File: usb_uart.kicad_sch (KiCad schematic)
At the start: 13 parts, among them J9 Conn_01x04_Female, U20 CP2102N-A01-GQFN28, U25 CM1293A-04SO

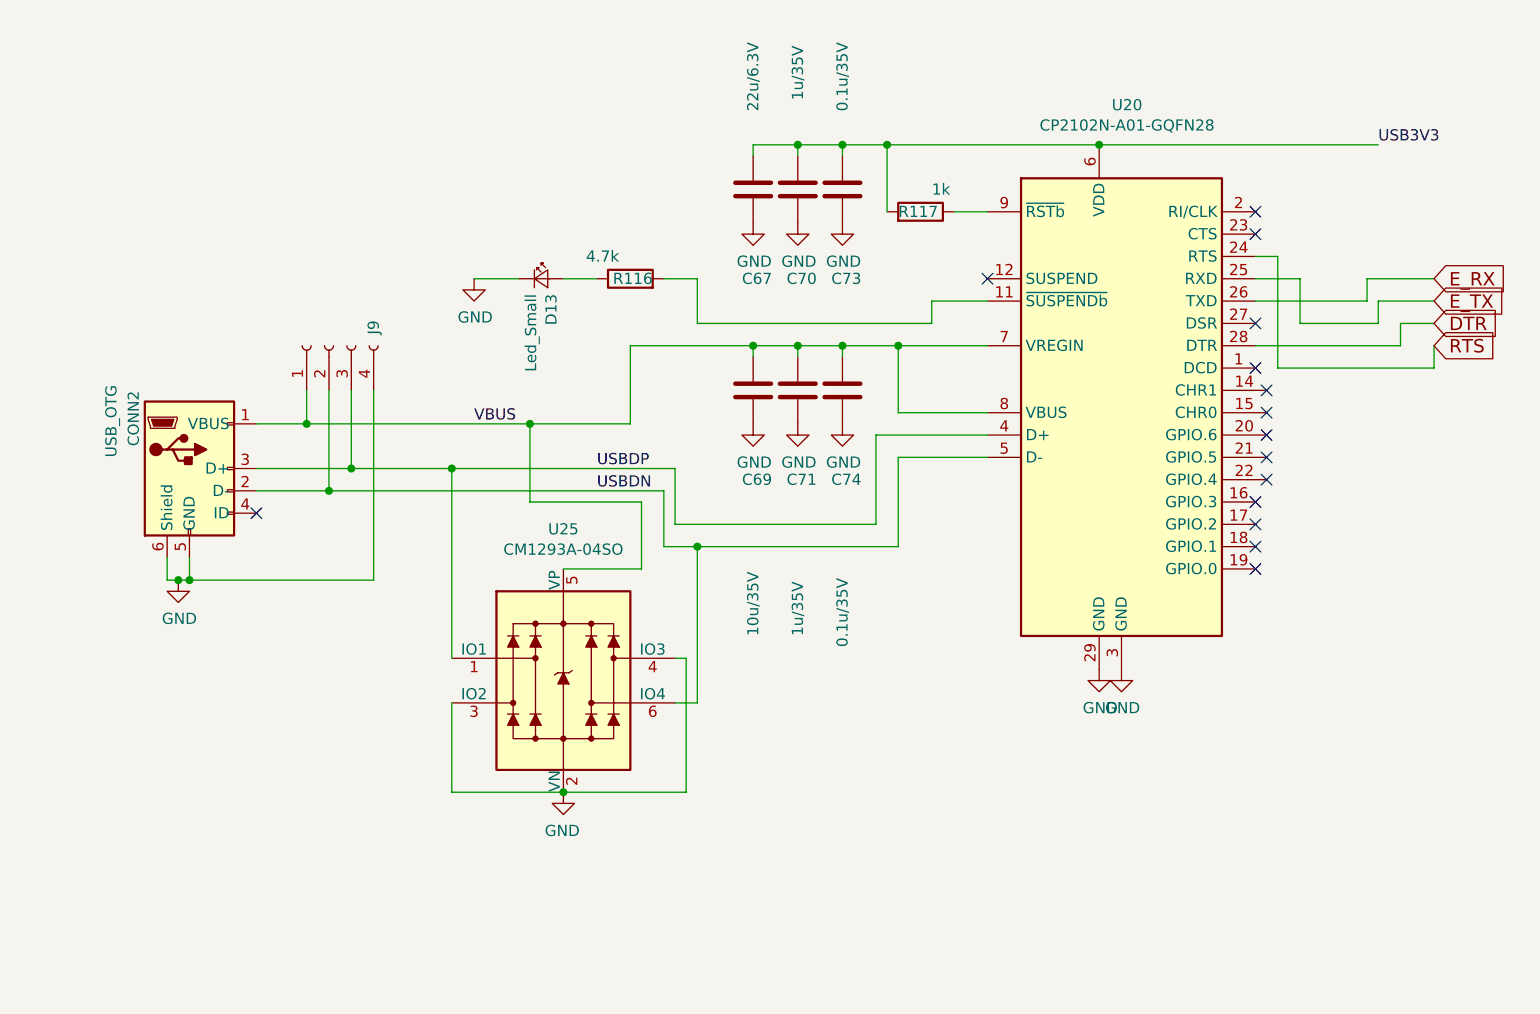
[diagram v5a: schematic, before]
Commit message: WROOM32 coupling capacitor order fixed; Added FB on long line to board left-most sensors
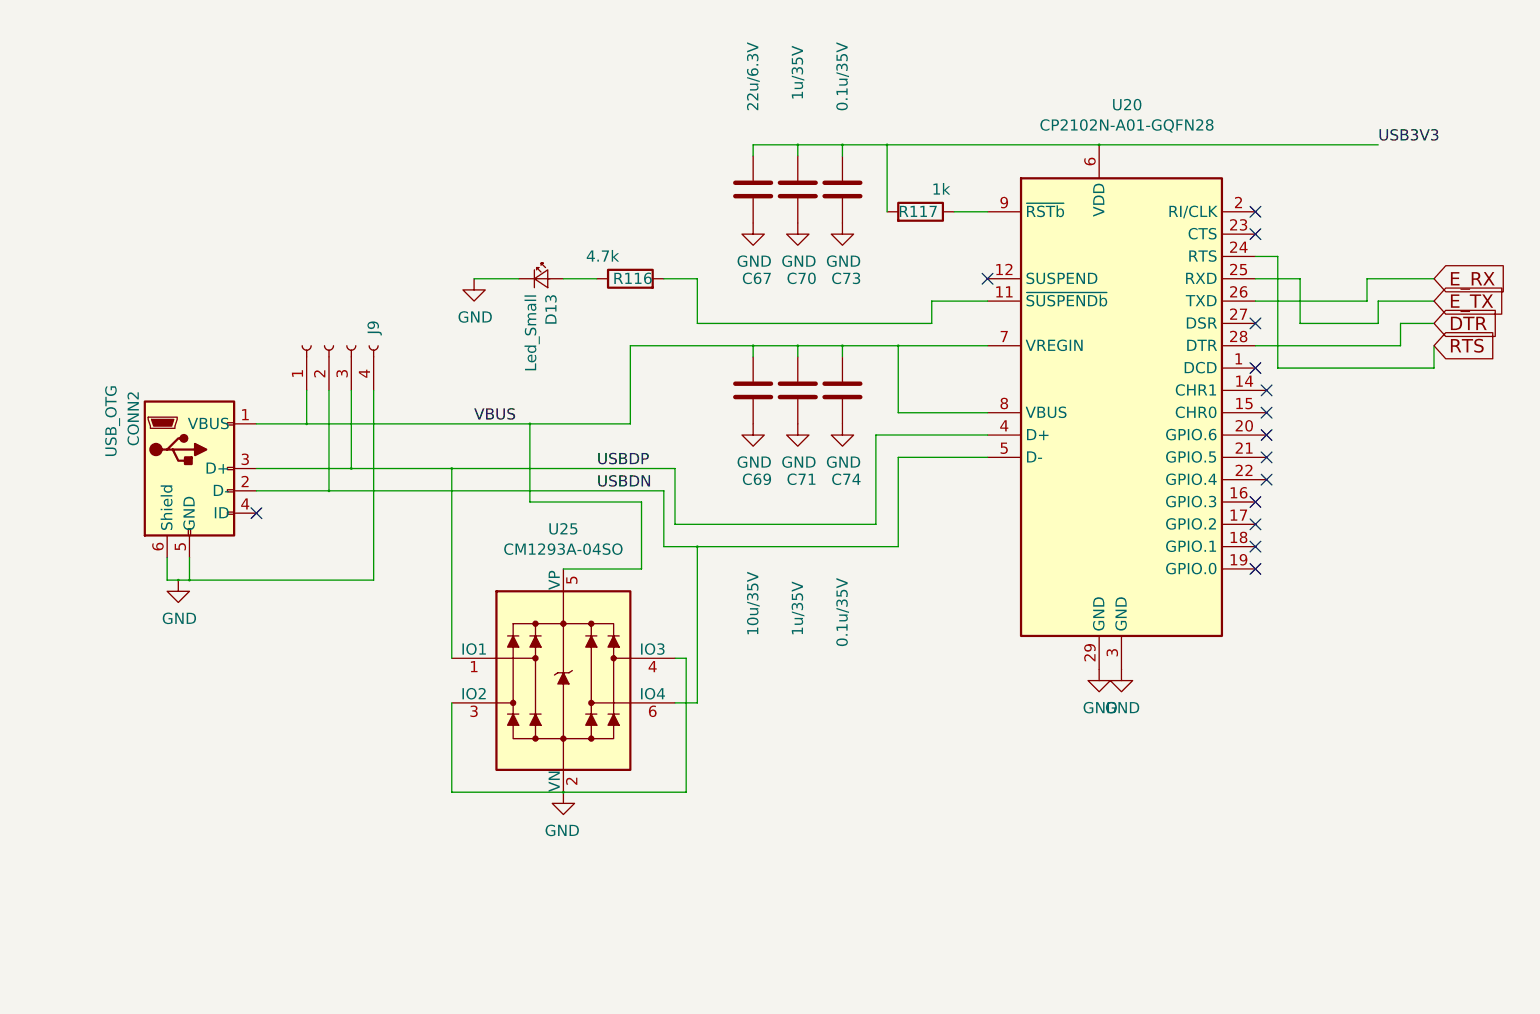
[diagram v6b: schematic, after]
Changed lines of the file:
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@@
-(kicad_sch (version 20200618) (host eeschema "5.99.0-unknown-7340c97~89~ubuntu18.04.1")
-  (page 1 10)
+(kicad_sch (version 20200714) (host eeschema "5.99.0-unknown-e5f2015a9~89~ubuntu18.04.1")
+  (page 10 10)
   (paper "A4")
-  (junction (at 31.115 81.28) (diameter 0) (color 0 0 0 0))
-  (junction (at 32.385 81.28) (diameter 0) (color 0 0 0 0))
-  (junction (at 45.72 63.5) (diameter 0) (color 0 0 0 0))
-  (junction (at 48.26 71.12) (diameter 0) (color 0 0 0 0))
-  (junction (at 50.8 68.58) (diameter 0) (color 0 0 0 0))
-  (junction (at 62.23 68.58) (diameter 0) (color 0 0 0 0))
-  (junction (at 71.12 63.5) (diameter 0) (color 0 0 0 0))
-  (junction (at 74.93 105.41) (diameter 0) (color 0 0 0 0))
-  (junction (at 90.17 77.47) (diameter 0) (color 0 0 0 0))
-  (junction (at 96.52 54.61) (diameter 0) (color 0 0 0 0))
-  (junction (at 101.6 31.75) (diameter 0) (color 0 0 0 0))
-  (junction (at 101.6 54.61) (diameter 0) (color 0 0 0 0))
-  (junction (at 106.68 31.75) (diameter 0) (color 0 0 0 0))
-  (junction (at 106.68 54.61) (diameter 0) (color 0 0 0 0))
-  (junction (at 111.76 31.75) (diameter 0) (color 0 0 0 0))
-  (junction (at 113.03 54.61) (diameter 0) (color 0 0 0 0))
-  (junction (at 135.89 31.75) (diameter 0) (color 0 0 0 0))
+  (junction (at 31.115 81.28) (diameter 0.3048) (color 0 0 0 0))
+  (junction (at 32.385 81.28) (diameter 0.3048) (color 0 0 0 0))
+  (junction (at 45.72 63.5) (diameter 0.3048) (color 0 0 0 0))
+  (junction (at 48.26 71.12) (diameter 0.3048) (color 0 0 0 0))
+  (junction (at 50.8 68.58) (diameter 0.3048) (color 0 0 0 0))
+  (junction (at 62.23 68.58) (diameter 0.3048) (color 0 0 0 0))
+  (junction (at 71.12 63.5) (diameter 0.3048) (color 0 0 0 0))
+  (junction (at 74.93 105.41) (diameter 0.3048) (color 0 0 0 0))
+  (junction (at 90.17 77.47) (diameter 0.3048) (color 0 0 0 0))
+  (junction (at 96.52 54.61) (diameter 0.3048) (color 0 0 0 0))
+  (junction (at 101.6 31.75) (diameter 0.3048) (color 0 0 0 0))
+  (junction (at 101.6 54.61) (diameter 0.3048) (color 0 0 0 0))
+  (junction (at 106.68 31.75) (diameter 0.3048) (color 0 0 0 0))
+  (junction (at 106.68 54.61) (diameter 0.3048) (color 0 0 0 0))
+  (junction (at 111.76 31.75) (diameter 0.3048) (color 0 0 0 0))
+  (junction (at 113.03 54.61) (diameter 0.3048) (color 0 0 0 0))
+  (junction (at 135.89 31.75) (diameter 0.3048) (color 0 0 0 0))
+  (no_connect (at 153.67 72.39))
+  (no_connect (at 123.19 46.99))
+  (no_connect (at 154.94 69.85))
+  (no_connect (at 153.67 57.15))
+  (no_connect (at 153.67 80.01))
+  (no_connect (at 153.67 77.47))
+  (no_connect (at 153.67 52.07))
+  (no_connect (at 154.94 64.77))
+  (no_connect (at 153.67 39.37))
+  (no_connect (at 153.67 74.93))
+  (no_connect (at 154.94 62.23))
   (no_connect (at 154.94 67.31))
-  (no_connect (at 153.67 77.47))
   (no_connect (at 154.94 59.69))
-  (no_connect (at 153.67 39.37))
-  (no_connect (at 153.67 80.01))
-  (no_connect (at 153.67 57.15))
   (no_connect (at 40.005 73.66))
   (no_connect (at 153.67 41.91))
-  (no_connect (at 153.67 74.93))
-  (no_connect (at 154.94 69.85))
-  (no_connect (at 153.67 72.39))
-  (no_connect (at 153.67 52.07))
-  (no_connect (at 154.94 64.77))
-  (no_connect (at 123.19 46.99))
-  (no_connect (at 154.94 62.23))
   (wire (pts (xy 29.845 81.28) (xy 29.845 78.74))
     (stroke (width 0) (type solid) (color 0 0 0 0))

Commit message: Changed from USB micro-B to Type C. DRC should be clear.
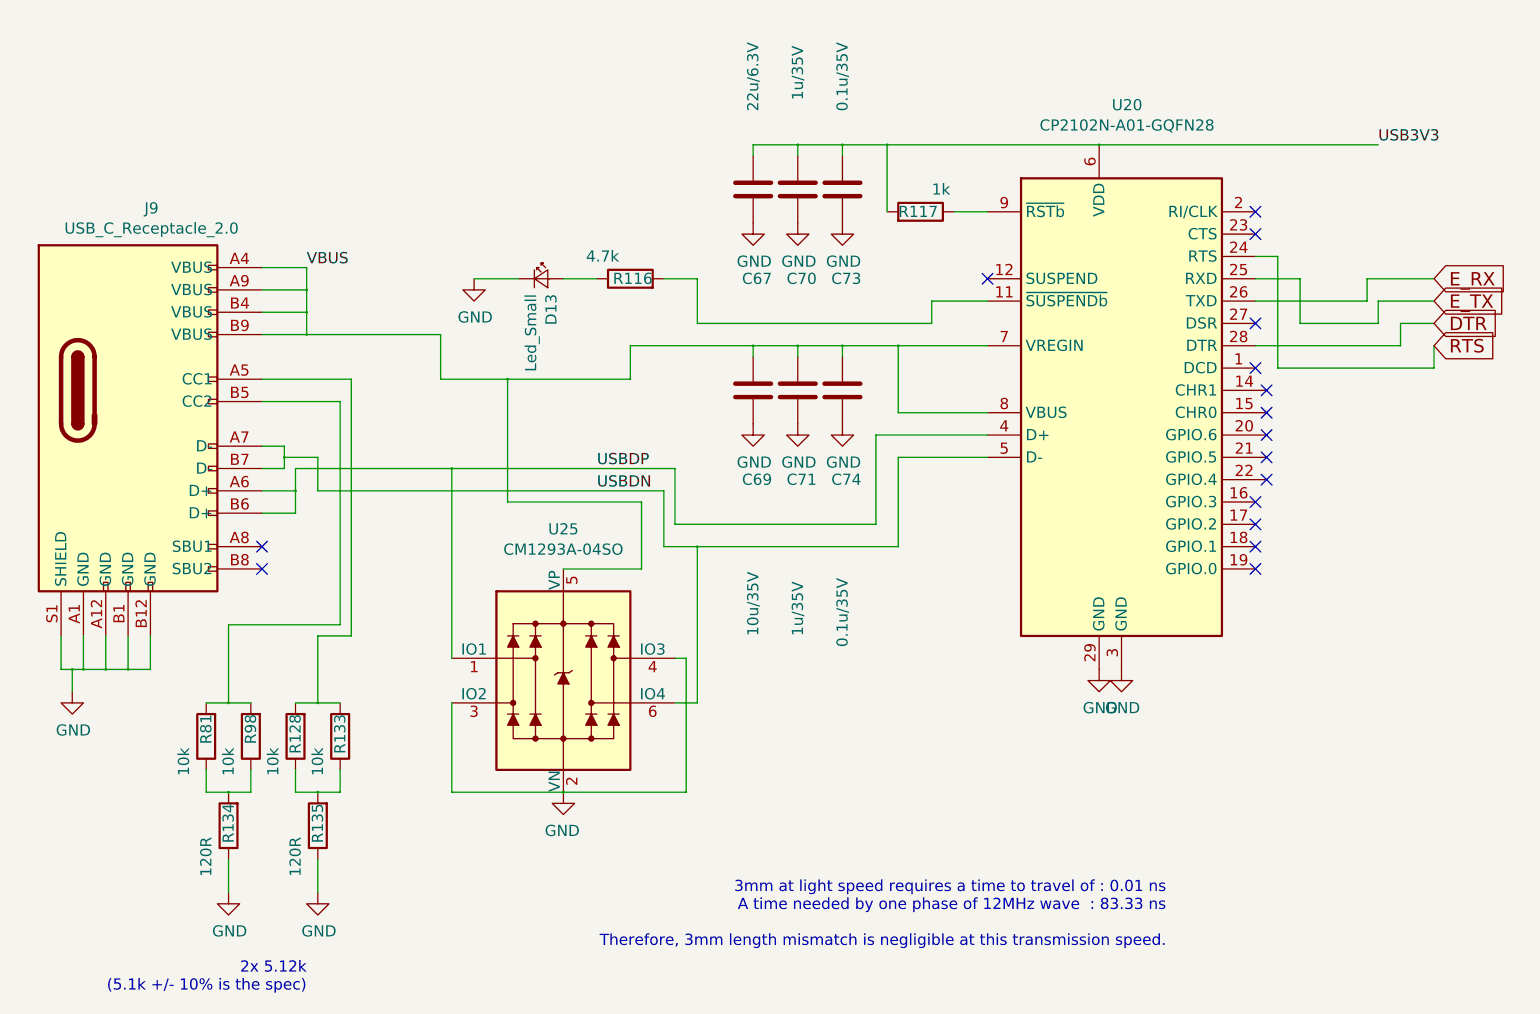
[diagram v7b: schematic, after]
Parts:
- removed CONN2: USB_OTG, components:USB_Micro-B_Jing_A01SB141B1-067, symbol dotmatrix_64x48-rescue:USB_OTG-Connector
- removed J9: Conn_01x04_Female, Connector_PinHeader_2.54mm:PinHeader_1x04_P2.54mm_Vertical, symbol dotmatrix_64x48-rescue:Conn_01x04_Female-Connector
- added J9: USB_C_Receptacle_2.0, components:DX07S016JA1R1500, symbol DeeComponents:USB_C_Receptacle_2.0
- added R128, R133, R81, R98: 10k, Resistor_SMD:R_0603_1608Metric_Pad1.05x0.95mm_HandSolder, symbol dotmatrix_64x48-rescue:R-device
- added R134, R135: 120R, Resistor_SMD:R_0603_1608Metric_Pad1.05x0.95mm_HandSolder, symbol dotmatrix_64x48-rescue:R-device
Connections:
- net GND: now also J9.A1 (GND), J9.A12 (GND), J9.B1 (GND), J9.B12 (GND), J9.S1 (SHIELD), R134.1, R135.1
- net USBDN: now also J9.A7 (D-), J9.B7 (D-)
- net USBDP: now also J9.A6 (D+), J9.B6 (D+)
- net VBUS: now also J9.A4 (VBUS), J9.A9 (VBUS), J9.B4 (VBUS), J9.B9 (VBUS)
- new net: R134.2, R81.1, R98.1
- new net: J9.B5 (CC2), R81.2, R98.2
- new net: R128.1, R133.1, R135.2
- new net: J9.A5 (CC1), R128.2, R133.2
- no-connect marks 15 -> 16
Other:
- note added: "2x 5.12k (5.1k +/- 10% is the spec)"
- note added: "3mm at light speed requires a time to travel of : 0.01 ns A time needed by one phase of 12MHz wave : 83.33 ns Therefore, 3mm length mismatch is negligible at this transmission speed."
